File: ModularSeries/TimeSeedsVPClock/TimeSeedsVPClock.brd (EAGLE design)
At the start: 80 x 46 mm, 53 parts

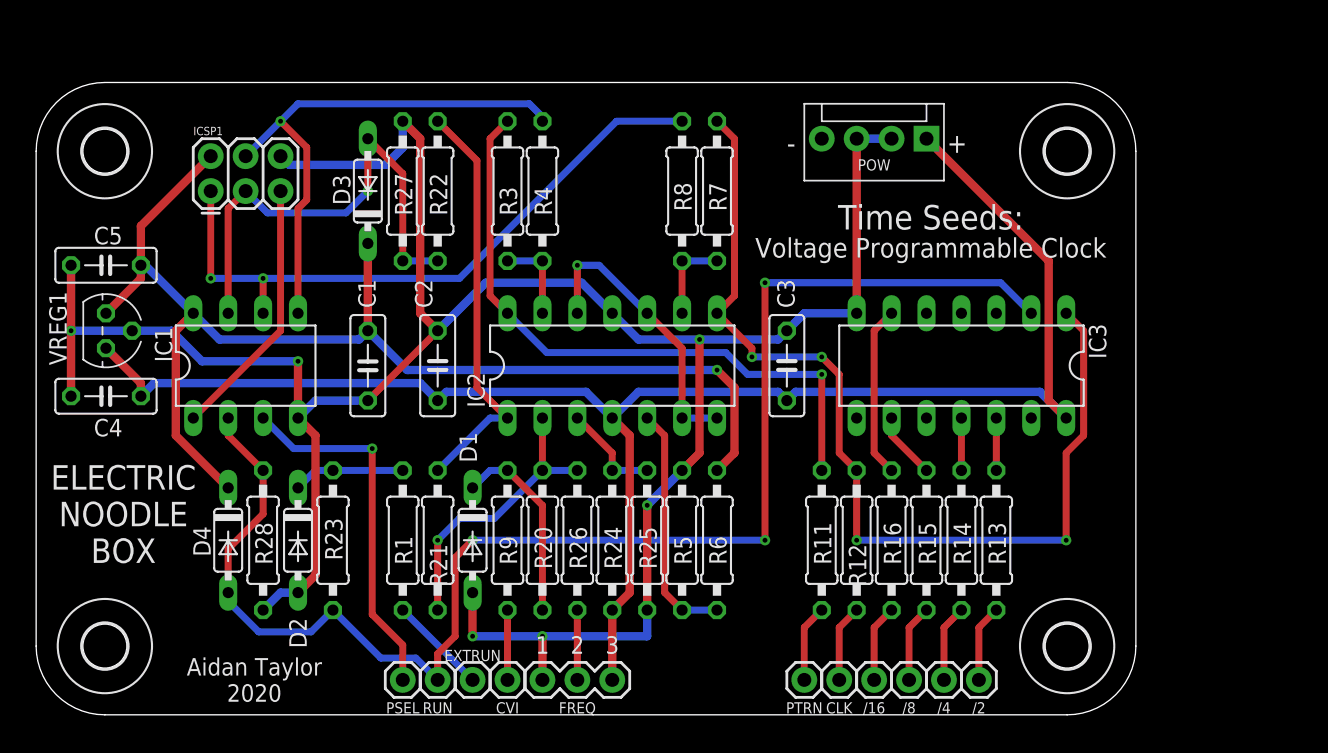
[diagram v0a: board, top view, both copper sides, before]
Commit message: Time Seeds VPC and TRHP SVG op-amps, schematics and layouts updated
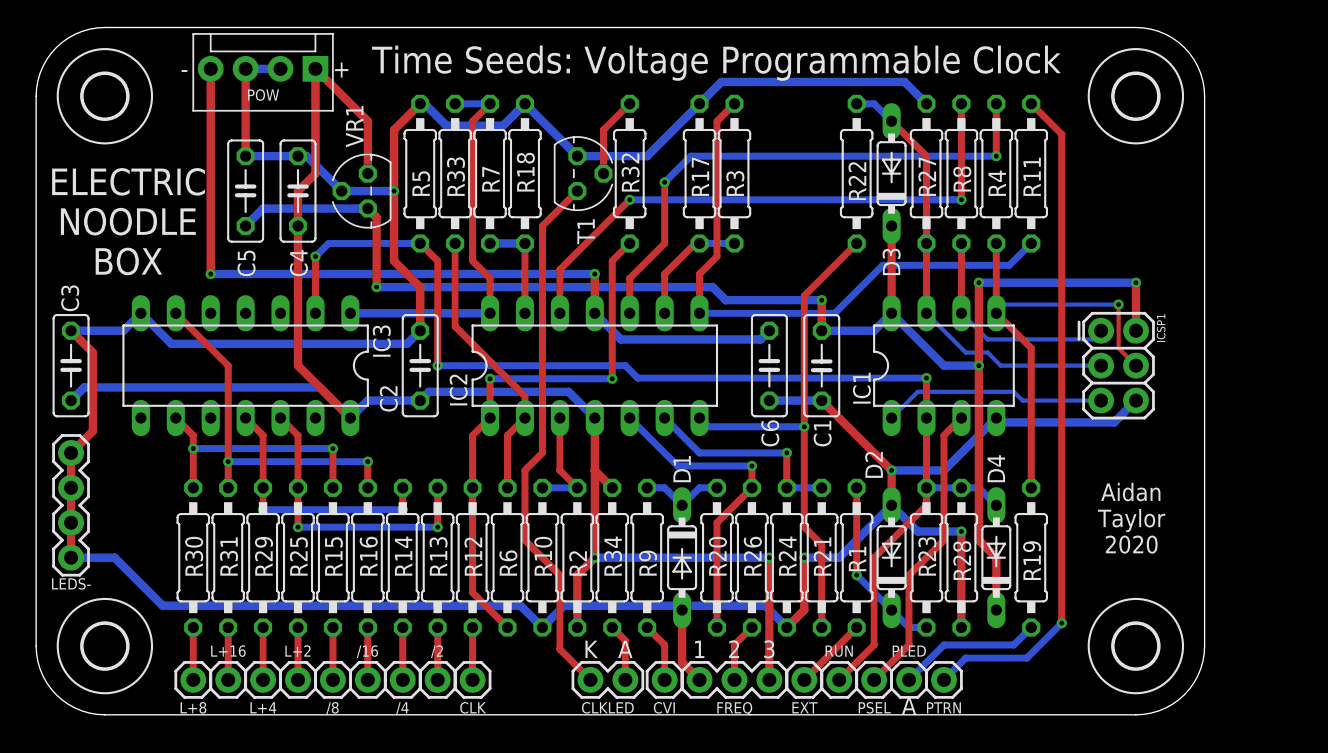
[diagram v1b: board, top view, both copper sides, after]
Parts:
- removed EXTRUN: 1XWIREPAD, ElectricNoodleBox:1X01
- removed VREG1: (no value), ElectricNoodleBox:TO92
- added C6: 100nF, rcl:C050-025X075
- added CLKLED: 2XWIREPAD, ElectricNoodleBox:1X02
- added EXT, L+16, L+2, L+4, L+8, PLED: 1XWIREPAD, ElectricNoodleBox:1X01
- added LEDS-: 4XWIREPAD, ElectricNoodleBox:1X04
- added R10, R17, R18, R33: 10K, rcl:0207/10
- added R19, R29, R30, R31: 470Ω, rcl:0207/10
- added R2: 14K, rcl:0207/10
- added R32: 100Ω, rcl:0207/10
- added R34: 1K, rcl:0207/10
- added T1: 2N3904, transistor:TO92
- added VR1: (no value), ElectricNoodleBox:TO92
- R25: value 100K -> 470Ω
- R9: value 1K -> 470Ω
- moved H2 83.2 mm to (80.0, 5.00)
- moved H1 70.0 mm to (5.00, 5.00)
- moved ICSP1 65.6 mm to (77.5, 27.9), turned to 270 degrees
- moved D4 55.9 mm to (69.8, 11.4), turned to 90 degrees
- moved C3 52.1 mm to (2.54, 25.4)
- moved IC3 52.1 mm to (15.2, 25.4)
- moved R28 50.8 mm to (67.3, 11.4)
- moved IC1 50.8 mm to (66.0, 25.4)
- moved POW 44.7 mm to (20.3, 47.0)
- moved D2 43.2 mm to (62.2, 11.4), turned to 90 degrees
- moved R15 43.2 mm to (21.6, 11.4)
- moved R23 43.2 mm to (64.8, 11.4), turned to 270 degrees
- moved /8 41.9 mm to (21.6, 2.54)
- moved R14 40.7 mm to (26.7, 11.4)
- moved R13 40.7 mm to (29.2, 11.4)
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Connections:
- new net N$12: IC2.1, R12.1, R32.1, R6.1
- new net N$22: IC2.3, R10.1, R2.2
- new net N$26: CLKLED.2, R34.1
- new net N$28: IC2.13, R18.2, R7.1
- new net N$33: IC2.14, IC3.1, R5.2, R7.2
- new net N$34: L+16.1, R31.2
- new net N$35: CLKLED.1, T1.1
- new net N$36: R32.2, T1.2
- net +12V: now also R2.1, R34.2, VR1.3; no longer R24.2, VREG1.3
- net +5V: now also VR1.1; no longer R6.2, VREG1.1
- net -12V: now also C6.2, IC2.11
- net AGND: now also C6.1, LEDS-.1, LEDS-.2, LEDS-.3, LEDS-.4, R10.2, R17.1, R18.1, R24.1, R33.1, T1.3, VR1.2; no longer IC2.11, R25.1, R5.1, VREG1.2
- net DRESET: now also R33.2
- net MOSI: now also R19.1
- net N$10: now also IC2.8, R11.1, R3.2; no longer IC2.10, IC2.12, IC2.6, IC2.7
- net N$13: now also R25.1
- net N$14: now also R29.1
- net N$15: now also R30.1
- net N$16: now also R31.1
- net N$17: now also L+2.1, R25.2; no longer IC3.5
- net N$18: now also L+4.1, R29.2; no longer IC3.4
- net N$19: now also L+8.1, R30.2; no longer IC3.3
- net N$2: now also EXT.1; no longer EXTRUN.1
- net N$20: now also IC2.5; no longer IC2.2, R21.1
- net N$21: now also IC2.7; no longer IC2.1
- net N$25: now also IC2.6, R21.1, R24.2; no longer IC2.3, R24.1, R25.2
- net N$4: now also IC2.10; no longer IC2.13, R3.1
- net N$5: now also IC2.9, R17.2, R3.1; no longer IC2.14, R11.1, R3.2
- net N$6: now also IC2.2, R5.1, R6.2; no longer IC2.5, R5.2, R6.1
- net N$8: now also IC2.12; no longer IC2.9, R7.1
- net N$9: now also PLED.1, R19.2; no longer IC2.8, IC3.1, R12.1, R7.2
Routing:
- net AGND: track 180.5 -> 247.9 mm, vias 6 -> 4
- net N$9: track 71.5 -> 10.5 mm, vias 4 -> 0
- net -12V: track 0.00 -> 59.5 mm, vias 0 -> 2
- net N$11: track 5.61 -> 49.0 mm, vias 0 -> 1
- net N$35: track 0.00 -> 39.1 mm
- net N$12: track 0.00 -> 38.9 mm, vias 0 -> 2
- net N$5: track 46.7 -> 8.86 mm, vias 1 -> 0
- net N$8: track 6.35 -> 41.5 mm, vias 0 -> 2
- net N$4: track 6.35 -> 39.3 mm, vias 0 -> 2
- net MISO: track 47.9 -> 16.3 mm, vias 2 -> 0
- net N$33: track 0.00 -> 29.0 mm
- net N$10: track 21.2 -> 42.5 mm, vias 1 -> 0
- net +5V: track 89.7 -> 109.5 mm, vias 1 -> 5
- net DRESET: track 105.9 -> 87.7 mm
- net N$13: track 3.81 -> 21.5 mm, vias 0 -> 2
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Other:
- board size 80 x 46 mm -> 85 x 50 mm
- board text added: "A"
- board text added: "K"
- board text added: "Time Seeds: Voltage Programmable Clock"
- board text removed: "Time Seeds:"
- board text removed: "Voltage Programmable Clock"

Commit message: CD4024 Reset fixed in Time Seeds
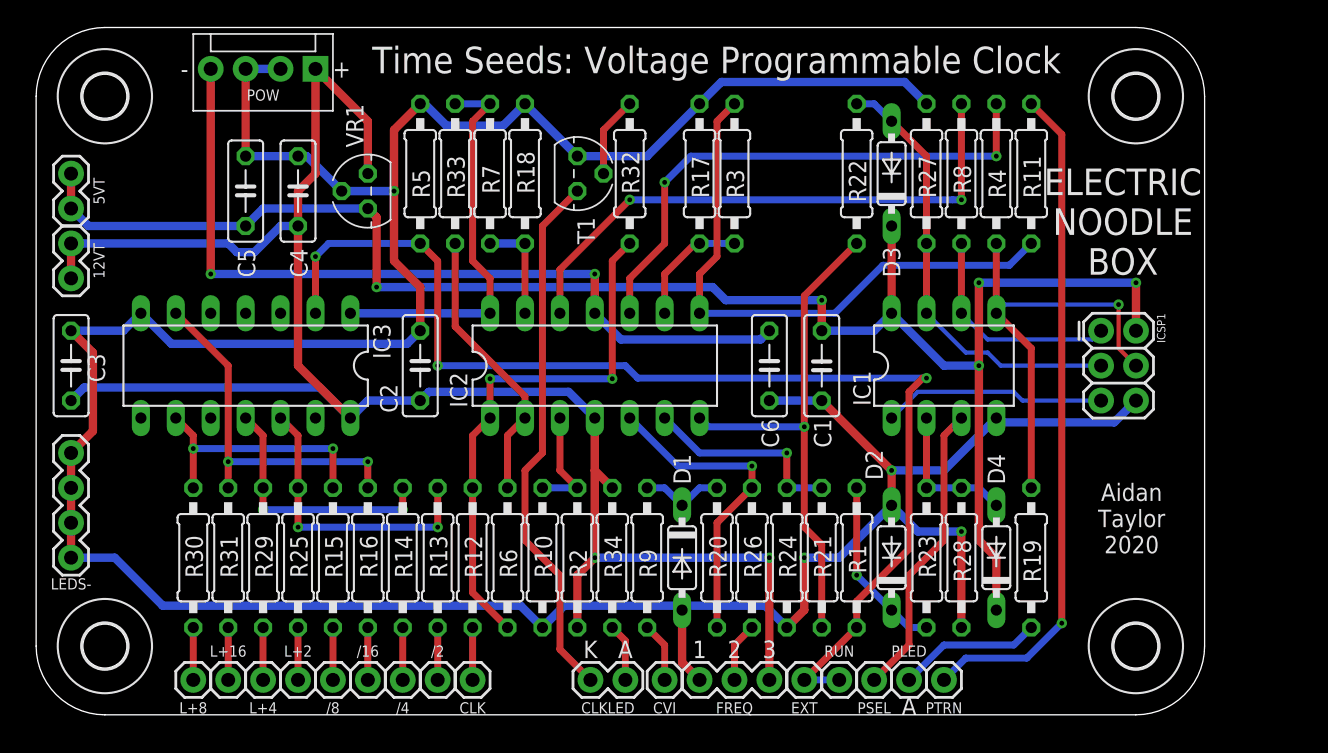
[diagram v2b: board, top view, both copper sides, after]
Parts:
- added 12VT, 5VT: 2XWIREPAD, ElectricNoodleBox:1X02
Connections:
- removed net N$2: EXT.1, R1.2
- new net NOTRES: D4.A, IC1.2, R23.1, R28.1
- net +12V: now also 12VT.1, 12VT.2
- net +5V: now also 5VT.1, 5VT.2
- net DRESET: now also EXT.1, R1.2; no longer D4.A, IC1.2, R23.1, R28.1
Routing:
- net +12V: track 116.8 -> 136.9 mm
- net +5V: track 109.5 -> 125.3 mm
- net NOTRES: track 0.00 -> 10.7 mm
- net N$2: track 5.39 -> 0.00 mm
- net DRESET: track 87.7 -> 85.8 mm
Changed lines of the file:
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@@
 <setting verticaltext="up"/>
 </settings>
-<grid distance="1" unitdist="mm" unit="mm" style="lines" multiple="1" display="no" altdistance="5" altunitdist="mil" altunit="mil"/>
+<grid distance="25" unitdist="mil" unit="mil" style="lines" multiple="1" display="no" altdistance="5" altunitdist="mil" altunit="mil"/>
 <layers>
 <layer number="1" name="Top" color="4" fill="1" visible="yes" active="yes"/>
@@
 <wire x1="5" y1="50" x2="0" y2="45" width="0" layer="20" curve="90"/>
 <text x="24.4475" y="46.6725" size="1.9304" layer="21" font="vector" ratio="16">Time Seeds: Voltage Programmable Clock</text>
-<text x="6.6675" y="35.8775" size="1.9304" layer="21" font="vector" ratio="16" align="center">ELECTRIC
+<text x="79.0575" y="35.8775" size="1.9304" layer="21" font="vector" ratio="16" align="center">ELECTRIC
 NOODLE
 BOX</text>
@@
 </element>
 <element name="C3" library="rcl" library_urn="urn:adsk.eagle:library:334" package="C050-025X075" package3d_urn="urn:adsk.eagle:package:23637/1" value="100nF" x="2.54" y="25.4" smashed="yes" rot="R90">
-<attribute name="NAME" x="3.1115" y="29.2735" size="1.27" layer="25" ratio="10" rot="R90"/>
+<attribute name="NAME" x="5.0165" y="24.1935" size="1.27" layer="25" ratio="10" rot="R90"/>
 <attribute name="POPULARITY" value="29" x="17.78" y="99.06" size="1.778" layer="27" rot="R90" display="off"/>
 <attribute name="SPICEPREFIX" value="C" x="17.78" y="99.06" size="1.778" layer="27" rot="R90" display="off"/>
@@
 <attribute name="SPICEPREFIX" value="R" x="41.91" y="11.43" size="1.778" layer="27" rot="R90" display="off"/>
 <attribute name="VALUE" x="42.545" y="9.1694" size="1.27" layer="27" ratio="10" rot="R90"/>
+</element>
+<element name="5VT" library="ElectricNoodleBox" package="1X02" value="2XWIREPAD" x="2.54" y="36.83" smashed="yes" rot="R90">
+<attribute name="NAME" x="4.572" y="38.1" size="0.8128" layer="25" font="vector" ratio="20" rot="R270" align="center"/>
+<attribute name="VALUE" x="0.762" y="36.83" size="0.6096" layer="27" font="vector" ratio="20" rot="R90"/>
+</element>
+<element name="12VT" library="ElectricNoodleBox" package="1X02" value="2XWIREPAD" x="2.54" y="31.75" smashed="yes" rot="R90">
+<attribute name="NAME" x="4.572" y="33.02" size="0.8128" layer="25" font="vector" ratio="20" rot="R270" align="center"/>
+<attribute name="VALUE" x="0.762" y="31.75" size="0.6096" layer="27" font="vector" ratio="20" rot="R90"/>
 </element>
 </elements>
@@
 <wire x1="15.24" y1="35.56" x2="16.51" y2="36.83" width="0.6096" layer="16"/>
 <wire x1="16.51" y1="36.83" x2="24.13" y2="36.83" width="0.6096" layer="16"/>
+<contactref element="5VT" pad="1"/>
+<contactref element="5VT" pad="2"/>
+<wire x1="15.24" y1="35.56" x2="3.81" y2="35.56" width="0.6096" layer="16"/>
+<wire x1="3.81" y1="35.56" x2="2.54" y2="36.83" width="0.6096" layer="16"/>
+<wire x1="2.54" y1="39.37" x2="2.54" y2="36.83" width="0.6096" layer="1"/>
 </signal>
 <signal name="N$8">
@@
 <signal name="DRESET">
 <contactref element="IC3" pad="2"/>
-<contactref element="IC1" pad="2"/>
-<contactref element="RUN" pad="1"/>
-<contactref element="R23" pad="1"/>
-<contactref element="R28" pad="1"/>
-<contactref element="D4" pad="A"/>
 <contactref element="R33" pad="2"/>
-<wire x1="58.42" y1="2.54" x2="60.96" y2="5.08" width="0.508" layer="1"/>
-<wire x1="60.96" y1="11.43" x2="64.77" y2="15.24" width="0.508" layer="1"/>
-<wire x1="64.77" y1="15.24" x2="64.77" y2="16.51" width="0.508" layer="1"/>
-<wire x1="60.96" y1="5.08" x2="60.96" y2="11.43" width="0.508" layer="1"/>
-<wire x1="64.77" y1="16.51" x2="67.31" y2="16.51" width="0.508" layer="16"/>
-<wire x1="67.31" y1="16.51" x2="68.58" y2="16.51" width="0.508" layer="16"/>
-<wire x1="68.58" y1="16.51" x2="69.85" y2="15.24" width="0.508" layer="16"/>
-<wire x1="64.77" y1="16.51" x2="64.77" y2="21.59" width="0.508" layer="1"/>
 <via x="64.77" y="24.4955" extent="1-16" drill="0.35"/>
 <wire x1="64.77" y1="24.4955" x2="43.767" y2="24.4955" width="0.508" layer="16"/>
@@
 <via x="29.21" y="25.4" extent="1-16" drill="0.35"/>
 <wire x1="29.21" y1="33.02" x2="27.94" y2="34.29" width="0.508" layer="1"/>
-<wire x1="64.77" y1="21.59" x2="64.77" y2="24.4955" width="0.508" layer="1"/>
 <wire x1="29.21" y1="25.4" x2="29.21" y2="33.02" width="0.508" layer="1"/>
 <via x="20.32" y="33.3375" extent="1-16" drill="0.35"/>
@@
 <wire x1="27.94" y1="34.29" x2="21.2725" y2="34.29" width="0.508" layer="16"/>
 <wire x1="21.2725" y1="34.29" x2="20.32" y2="33.3375" width="0.508" layer="16"/>
+<contactref element="EXT" pad="1"/>
+<contactref element="R1" pad="2"/>
+<wire x1="55.88" y1="2.54" x2="59.69" y2="6.35" width="0.508" layer="1"/>
+<contactref element="RUN" pad="1"/>
+<wire x1="58.42" y1="2.54" x2="55.88" y2="2.54" width="0.508" layer="16"/>
+<wire x1="59.69" y1="6.35" x2="59.69" y2="8.255" width="0.508" layer="1"/>
+<wire x1="59.69" y1="8.255" x2="63.5" y2="12.065" width="0.508" layer="1"/>
+<wire x1="63.5" y1="12.065" x2="63.5" y2="23.495" width="0.508" layer="1"/>
+<wire x1="63.5" y1="23.495" x2="64.5005" y2="24.4955" width="0.508" layer="1"/>
+<wire x1="64.5005" y1="24.4955" x2="64.77" y2="24.4955" width="0.508" layer="1"/>
 </signal>
 <signal name="N$13">
@@
 <wire x1="19.05" y1="38.1" x2="20.32" y2="39.37" width="0.6096" layer="1"/>
 <wire x1="20.32" y1="39.37" x2="20.32" y2="46.99" width="0.6096" layer="1"/>
+<contactref element="12VT" pad="1"/>
+<contactref element="12VT" pad="2"/>
+<wire x1="19.05" y1="35.56" x2="17.78" y2="35.56" width="0.6096" layer="16"/>
+<wire x1="17.78" y1="35.56" x2="15.875" y2="33.655" width="0.6096" layer="16"/>
+<wire x1="15.875" y1="33.655" x2="14.605" y2="33.655" width="0.6096" layer="16"/>
+<wire x1="14.605" y1="33.655" x2="13.97" y2="34.29" width="0.6096" layer="16"/>
+<wire x1="13.97" y1="34.29" x2="2.54" y2="34.29" width="0.6096" layer="16"/>
+<wire x1="2.54" y1="34.29" x2="2.54" y2="31.75" width="0.6096" layer="1"/>
 </signal>
 <signal name="SCK">
@@
 <wire x1="45.72" y1="5.08" x2="44.45" y2="6.35" width="0.508" layer="1"/>
 </signal>
-<signal name="N$2">
-<contactref element="EXT" pad="1"/>
-<contactref element="R1" pad="2"/>
-<wire x1="55.88" y1="2.54" x2="59.69" y2="6.35" width="0.508" layer="1"/>
-</signal>
 <signal name="N$7">
 <contactref element="R1" pad="1"/>
@@
 <wire x1="41.275" y1="42.545" x2="43.18" y2="44.45" width="0.508" layer="1"/>
 </signal>
+<signal name="NOTRES">
+<contactref element="IC1" pad="2"/>
+<contactref element="R23" pad="1"/>
+<contactref element="R28" pad="1"/>
+<contactref element="D4" pad="A"/>
+<wire x1="64.77" y1="16.51" x2="67.31" y2="16.51" width="0.508" layer="16"/>
+<wire x1="67.31" y1="16.51" x2="68.58" y2="16.51" width="0.508" layer="16"/>
+<wire x1="68.58" y1="16.51" x2="69.85" y2="15.24" width="0.508" layer="16"/>
+<wire x1="64.77" y1="16.51" x2="64.77" y2="21.59" width="0.508" layer="1"/>
+</signal>
 </signals>
